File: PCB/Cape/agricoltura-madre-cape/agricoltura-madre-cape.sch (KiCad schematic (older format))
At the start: 0 parts

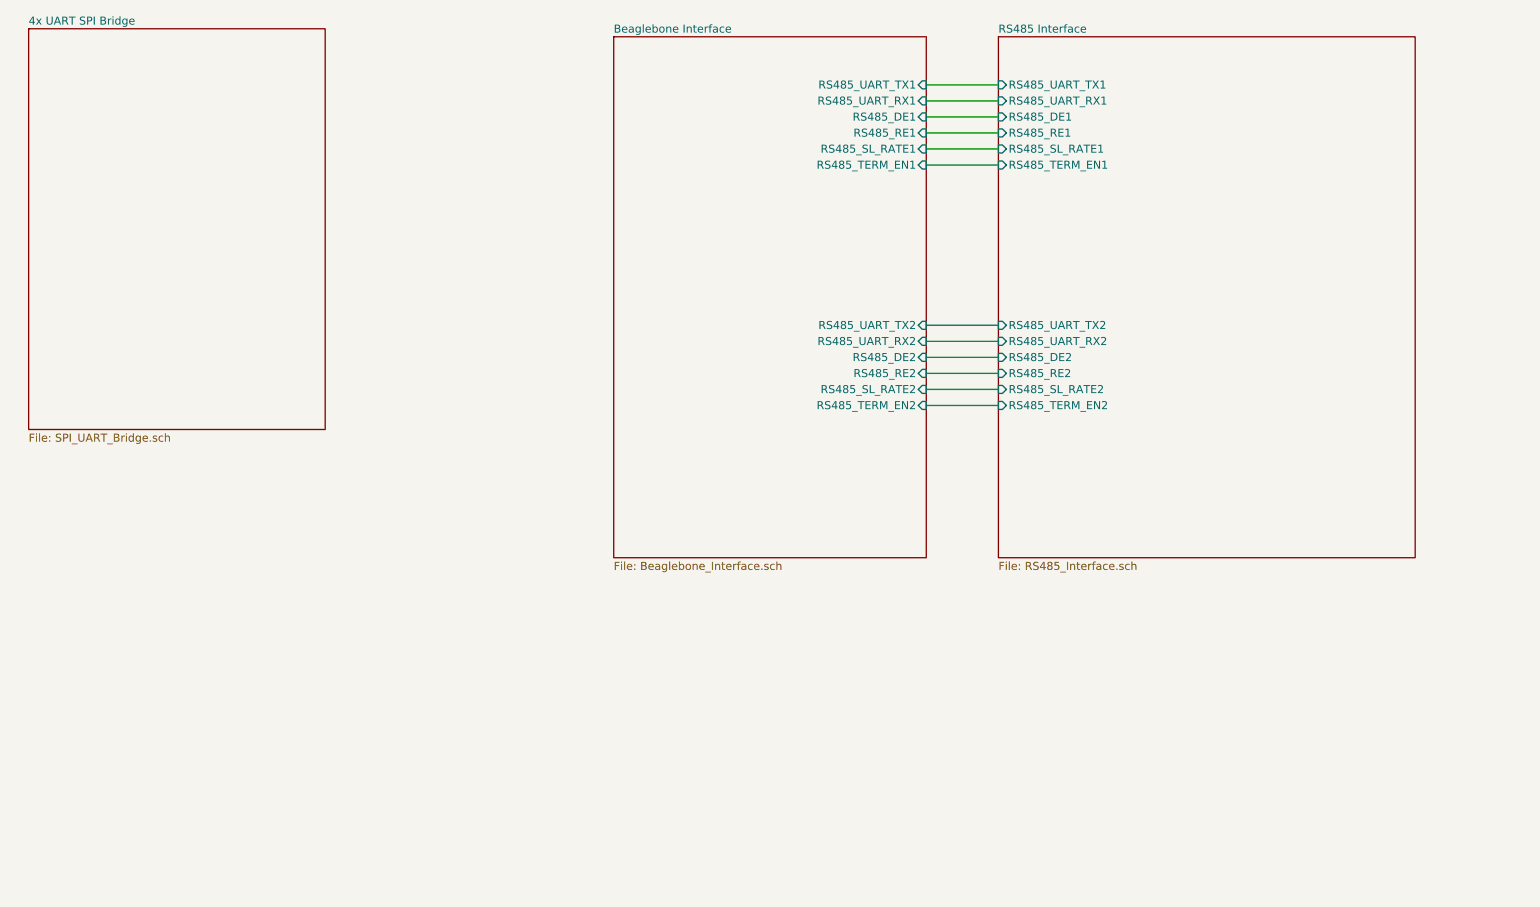
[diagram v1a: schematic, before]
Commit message: SPI UART Bridge
Fleshed out schematic for SPI UART bridge chip, realized we may not need it, now going to fork project and develop two versions in this same repository.
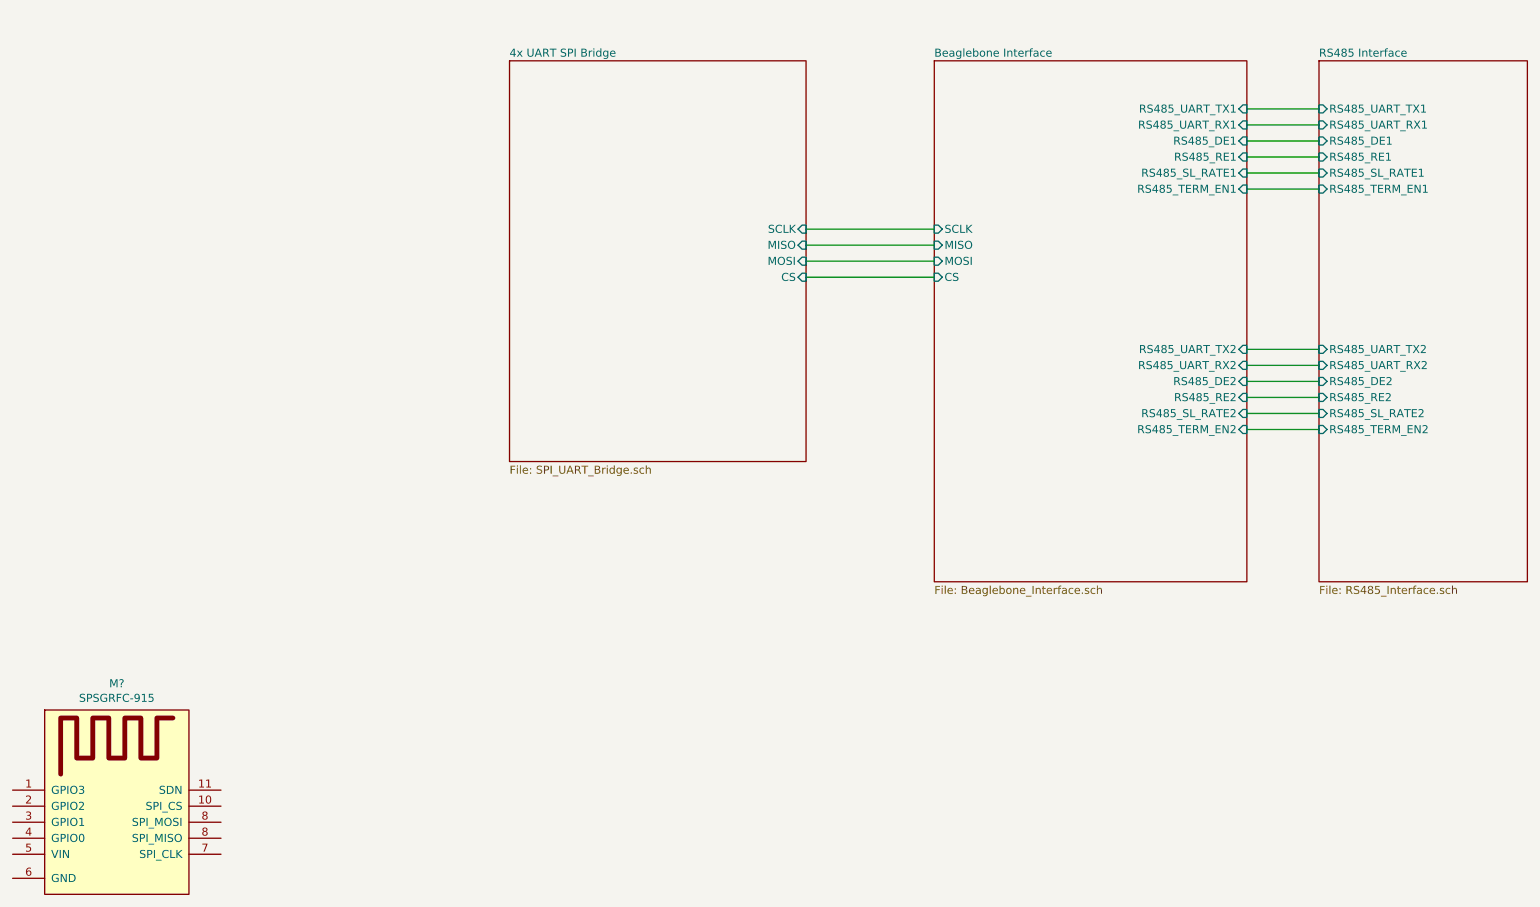
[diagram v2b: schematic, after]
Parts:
- added M?: SPSGRFC-915, AVR-KiCAD-Lib-Modules:XCVR_SPSGRF-915, symbol AVR-KiCAD-Lib-Modules:SPSGRFC-915
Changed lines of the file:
@@
 $EndDescr
 $Sheet
-S 5300 1750 1950 3250
+S 7300 1900 1950 3250
 U 5EFF01A0
 F0 "Beaglebone Interface" 50
 F1 "Beaglebone_Interface.sch" 50
-F2 "RS485_UART_TX1" I R 7250 2050 50
-F3 "RS485_UART_RX1" I R 7250 2150 50
-F4 "RS485_UART_TX2" I R 7250 3550 50
-F5 "RS485_UART_RX2" I R 7250 3650 50
-F6 "RS485_DE2" I R 7250 3750 50
-F7 "RS485_DE1" I R 7250 2250 50
-F8 "RS485_SL_RATE2" I R 7250 3950 50
-F9 "RS485_SL_RATE1" I R 7250 2450 50
-F10 "RS485_TERM_EN1" I R 7250 2550 50
-F11 "RS485_RE1" I R 7250 2350 50
-F12 "RS485_RE2" I R 7250 3850 50
-F13 "RS485_TERM_EN2" I R 7250 4050 50
+F2 "RS485_UART_TX1" I R 9250 2200 50
+F3 "RS485_UART_RX1" I R 9250 2300 50
+F4 "RS485_UART_TX2" I R 9250 3700 50
+F5 "RS485_UART_RX2" I R 9250 3800 50
+F6 "RS485_DE2" I R 9250 3900 50
+F7 "RS485_DE1" I R 9250 2400 50
+F8 "RS485_SL_RATE2" I R 9250 4100 50
+F9 "RS485_SL_RATE1" I R 9250 2600 50
+F10 "RS485_TERM_EN1" I R 9250 2700 50
+F11 "RS485_RE1" I R 9250 2500 50
+F12 "RS485_RE2" I R 9250 4000 50
+F13 "RS485_TERM_EN2" I R 9250 4200 50
+F14 "SCLK" I L 7300 2950 50
+F15 "MISO" I L 7300 3050 50
+F16 "MOSI" I L 7300 3150 50
+F17 "CS" I L 7300 3250 50
 $EndSheet
 $Sheet
-S 7700 1750 2600 3250
+S 9700 1900 1300 3250
 U 5EFF8157
 F0 "RS485 Interface" 50
 F1 "RS485_Interface.sch" 50
-F2 "RS485_UART_TX1" I L 7700 2050 50
-F3 "RS485_UART_RX1" I L 7700 2150 50
-F4 "RS485_UART_TX2" I L 7700 3550 50
-F5 "RS485_UART_RX2" I L 7700 3650 50
-F6 "RS485_DE2" I L 7700 3750 50
-F7 "RS485_DE1" I L 7700 2250 50
-F8 "RS485_SL_RATE2" I L 7700 3950 50
-F9 "RS485_SL_RATE1" I L 7700 2450 50
-F10 "RS485_TERM_EN1" I L 7700 2550 50
-F11 "RS485_RE1" I L 7700 2350 50
-F12 "RS485_RE2" I L 7700 3850 50
-F13 "RS485_TERM_EN2" I L 7700 4050 50
+F2 "RS485_UART_TX1" I L 9700 2200 50
+F3 "RS485_UART_RX1" I L 9700 2300 50
+F4 "RS485_UART_TX2" I L 9700 3700 50
+F5 "RS485_UART_RX2" I L 9700 3800 50
+F6 "RS485_DE2" I L 9700 3900 50
+F7 "RS485_DE1" I L 9700 2400 50
+F8 "RS485_SL_RATE2" I L 9700 4100 50
+F9 "RS485_SL_RATE1" I L 9700 2600 50
+F10 "RS485_TERM_EN1" I L 9700 2700 50
+F11 "RS485_RE1" I L 9700 2500 50
+F12 "RS485_RE2" I L 9700 4000 50
+F13 "RS485_TERM_EN2" I L 9700 4200 50
 $EndSheet
 Wire Wire Line
-	7250 2050 7700 2050
+	9250 2200 9700 2200
 Wire Wire Line
-	7250 2150 7700 2150
+	9250 2300 9700 2300
 Wire Wire Line
-	7250 2250 7700 2250
+	9250 2400 9700 2400
 Wire Wire Line
-	7250 2350 7700 2350
+	9250 2500 9700 2500
 Wire Wire Line
-	7700 2450 7250 2450
+	9700 2600 9250 2600
 Wire Wire Line
-	7250 2550 7700 2550
+	9250 2700 9700 2700
 Wire Wire Line
-	7250 3550 7700 3550
+	9250 3700 9700 3700
 Wire Wire Line
-	7250 3650 7700 3650
+	9250 3800 9700 3800
 Wire Wire Line
-	7700 3750 7250 3750
+	9700 3900 9250 3900
 Wire Wire Line
-	7250 3850 7700 3850
+	9250 4000 9700 4000
 Wire Wire Line
-	7700 3950 7250 3950
+	9700 4100 9250 4100
 Wire Wire Line
-	7250 4050 7700 4050
+	9250 4200 9700 4200
 $Sheet
-S 1650 1700 1850 2500
+S 4650 1900 1850 2500
 U 5EFE97F6
 F0 "4x UART SPI Bridge" 50
 F1 "SPI_UART_Bridge.sch" 50
+F2 "SCLK" I R 6500 2950 50
+F3 "MISO" I R 6500 3050 50
+F4 "MOSI" I R 6500 3150 50
+F5 "CS" I R 6500 3250 50
 $EndSheet
+Wire Wire Line
+	7300 3250 6500 3250
+Wire Wire Line
+	6500 3050 7300 3050
+Wire Wire Line
+	6500 3150 7300 3150
+Wire Wire Line
+	7300 2950 6500 2950
+$Comp
+L AVR-KiCAD-Lib-Modules:SPSGRFC-915 M?
+U 1 1 5F1094AC
+P 1750 5950
+F 0 "M?" H 2200 6115 50  0000 C CNN
+F 1 "SPSGRFC-915" H 1800 6150 50  0001 C CNN
+F 2 "AVR-KiCAD-Lib-Modules:XCVR_SPSGRF-915" H 3800 8700 50  0001 C CNN
+F 3 "https://www.st.com/content/ccc/resource/technical/document/datasheet/group3/21/ae/a6/78/64/3b/46/5d/DM00347814/files/DM00347814.pdf/jcr:content/translations/en.DM00347814.pdf" H 1650 6050 50  0001 C CNN
+F 4 "12.35000" H 1850 6200 50  0001 C CNN "Cost QTY: 1"
+F 5 "7.82040" H 1950 6300 50  0001 C CNN "Cost QTY: 1000"
+F 6 "*" H 2050 6400 50  0001 C CNN "Cost QTY: 2500"
+F 7 "7.29120" H 2150 6500 50  0001 C CNN "Cost QTY: 5000"
+F 8 "7.05600" H 2250 6600 50  0001 C CNN "Cost QTY: 10000"
+F 9 "STMicroelectronics" H 2350 6700 50  0001 C CNN "MFR"
+F 10 "SPSGRFC-915" H 2450 6800 50  0001 C CNN "MFR#"
+F 11 "Digikey" H 2550 6900 50  0001 C CNN "Vendor"
+F 12 "497-17226-ND" H 2650 7000 50  0001 C CNN "Vendor #"
+F 13 "AVR" H 2750 7100 50  0001 C CNN "Designer"
+F 14 "2mm" H 2850 7200 50  0001 C CNN "Height"
+F 15 "6/4/2020" H 3950 8300 50  0001 C CNN "Date Created"
+F 16 "6/4/2020" H 2950 7300 50  0001 C CNN "Date Modified"
+F 17 "Yes" H 3050 7400 50  0001 C CNN "Lead-Free ?"
+F 18 "1" H 3150 7500 50  0001 C CNN "RoHS Levels"
+F 19 "SMT" H 3250 7600 50  0001 C CNN "Mounting"
+F 20 "11" H 3350 7700 50  0001 C CNN "Pin Count #"
+F 21 "Active" H 3450 7800 50  0001 C CNN "Status"
+F 22 "*" H 3550 7900 50  0001 C CNN "Tolerance"
+F 23 "SoM" H 3650 8000 50  0001 C CNN "Type"
+F 24 "1.8V ~ 3.6V" H 3750 8100 50  0001 C CNN "Voltage"
+F 25 "Proprietary Module" H 3850 8250 50  0001 C CNN "Package"
+F 26 "General ISM < 1GHz  Transceiver Module 433MHz, 868MHz, 915MHz Antenna Not Included, U.FL Surface Mount" H 4150 8550 50  0001 C CNN "Description"
+F 27 "SPSGRFC-915" H 2200 6024 50  0000 C CNN "_Value_"
+F 28 "*" H 4150 8550 50  0001 C CNN "Management_ID"
+	1    1750 5950
+	1    0    0    -1
+$EndComp
 $EndSCHEMATC
